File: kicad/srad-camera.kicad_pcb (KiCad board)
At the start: 4 copper layers, 265 parts, among them J1 DEBUG, U1 AP61300Z6, U2 AP61300Z6, U3 RK809-5, U4 STM32U575RGT6, U5 RK3566, U6 MT41K256M16TW-107:P

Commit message: Finished wiring PMIC, STM, power input, IMU, FPC
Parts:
- removed the C43 at (254.5, 70.2)
- removed the C43 at (252.2, 70.5)
- added C43: 22uF, Capacitor_SMD:C_1206_3216Metric, B.Cu at (250.1, 57.5)
- C18, C21, C22, C50, C51: moved to F.Cu
- C2, C20, C3, C38, C39, C4, C40, C41, C42, C44, C45, C49, C5, C52, C53, C54, C55, C56, C57, C58, C59, C60, C61, C62, C63, R30, R33, R34: moved to B.Cu
- moved R1 134.1 mm to (207.0, 69.5), turned to 90 degrees
- moved R2 134.0 mm to (207.1, 65.1), turned to 90 degrees
- moved C128 130.6 mm to (169.0, 101.7)
- moved C129 130.6 mm to (165.5, 101.4)
- moved C130 130.6 mm to (165.5, 103.4)
- moved C131 130.6 mm to (165.5, 105.3)
- moved C132 130.6 mm to (165.5, 107.3)
- moved C133 130.6 mm to (165.5, 109.3)
- moved C134 130.6 mm to (165.5, 111.2)
- moved C135 130.6 mm to (165.5, 113.2)
- moved C136 130.6 mm to (165.5, 115.2)
- moved R49 130.6 mm to (168.4, 103.9)
- moved R3 129.7 mm to (202.5, 75.2), turned to -90 degrees
- moved C53 129.1 mm to (199.8, 67.7), turned to 180 degrees
- moved R32 125.6 mm to (201.5, 75.2), turned to 90 degrees
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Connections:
- C124 pad 2: /RK3566 SoC/VCC_1V8 -> /RK809-5 PMIC/FB4
- C39 pad 1: /RK809-5 PMIC/FB5 -> BUCK5_2V2
- C40 pad 1: /RK809-5 PMIC/FB5 -> BUCK5_2V2
- C41 pad 1: /RK809-5 PMIC/FB5 -> BUCK5_2V2
- C51 pad 2: VCC_3V3_SYS -> /RK809-5 PMIC/VCC_RTC
- L6 pad 2: /RK809-5 PMIC/FB5 -> BUCK5_2V2
- U3 pad 45: VCC_3V3_SYS -> /RK809-5 PMIC/VCC_RTC
- U3 pad 59: /RK809-5 PMIC/FB5 -> BUCK5_2V2
- U5 pad 1C13: /RK3566 SoC/VCC_1V8 -> /RK809-5 PMIC/FB4
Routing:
- net GND: track 34.6 -> 88.8 mm, vias 30 -> 93
- net BUCK5_2V2: track 19.8 -> 56.3 mm, vias 2 -> 5
- net /PMIC_INT: track 7.44 -> 26.2 mm, vias 1 -> 2
- net /PMIC_CLK: track 1.77 -> 20.1 mm, vias 1 -> 0
- net /PMIC_SDA: track 5.60 -> 23.1 mm
- net /RK809-5 PMIC/FB4: track 0.00 -> 17.2 mm, vias 0 -> 2
- net /PMIC_SCL: track 6.08 -> 22.6 mm
- net /RK809-5 PMIC/VBUCK3: track 6.47 -> 21.4 mm, vias 0 -> 3
- net /STM32U575RGT6/SWDIO: track 16.6 -> 3.29 mm
- net /STM32U575RGT6/SWO: track 11.3 -> 1.86 mm
- net /RK3566 SoC/VCCA_1V8_PMU: track 1.69 -> 10.5 mm, vias 0 -> 1
- net /STM32U575RGT6/SWCLK: track 10.6 -> 1.97 mm
- net /Power Supply/VIN_5V: track 17.1 -> 8.90 mm, vias 0 -> 4
- net VCCIO_3V3_IMU: track 15.3 -> 8.29 mm, vias 1 -> 3
- net /LSM6DSRTR/SDA: track 11.3 -> 4.46 mm, vias 2 -> 1
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- added copper zone on B.Cu, net GND
- added copper zone on F.Cu, net GND

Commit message: WIP PCB layout
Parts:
- removed D1: SMAJ5.0A, Diode_SMD:D_SMA
- added H1: MntHole, srad-camera-footprints:4-40_MountingHole, F.Cu at (125.0, 80.5)
- added H2: MntHole, srad-camera-footprints:4-40_MountingHole, F.Cu at (167.0, 80.5)
- added H3: MntHole, srad-camera-footprints:4-40_MountingHole, F.Cu at (125.0, 122.5)
- added H4: MntHole, srad-camera-footprints:4-40_MountingHole, F.Cu at (167.0, 122.5)
- added SW1: POWER, Button_Switch_SMD:SW_SPDT_PCM12, F.Cu at (66.0, 61.1)
- added SW2: USER, Button_Switch_SMD:SW_SPST_EVQP2_MiddlePushTravel_H2.5mm, F.Cu at (65.1, 74.5)
- added SW3: BOOT0, Button_Switch_SMD:SW_SPDT_PCM12, F.Cu at (66.0, 68.0)
- C1, FB1, FPC1, IMU1, R6, R7, SD1: moved to B.Cu
- C62, C63, R33, R34: moved to F.Cu
- J1: footprint Connector_PinHeader_1.27mm:PinHeader_2x05_P1.27mm_Vertical_SMD -> Connector_PinHeader_1.27mm:PinHeader_2x03_P1.27mm_Vertical
- USB1: footprint srad-camera-footprints:USB-SMD_TYPE-C16PIN-1 -> Connector_USB:USB_C_Receptacle_G-Switch_GT-USB-7010ASV
- moved C10 113.9 mm to (149.2, 85.5)
- moved C13 113.9 mm to (149.6, 83.0)
- moved C17 113.9 mm to (151.2, 93.9)
- moved C30 113.9 mm to (151.3, 92.7)
- moved L4 113.9 mm to (153.9, 85.6)
- moved R21 113.9 mm to (151.2, 92.0)
- moved R22 113.9 mm to (152.9, 83.2)
- moved R23 113.9 mm to (154.4, 83.2)
- moved C11 113.9 mm to (143.3, 86.8)
- moved C12 113.9 mm to (150.2, 88.0)
- moved C14 113.9 mm to (143.5, 88.6)
- moved C15 113.9 mm to (143.3, 85.1)
- moved C16 113.9 mm to (143.9, 83.4)
- moved C18 113.9 mm to (144.5, 92.6)
- moved C19 113.9 mm to (143.1, 94.1)
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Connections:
- net /RK3566 SoC/MIPI_DN0 renamed /RK3566 SoC/MIPI_D0_N
- net /RK3566 SoC/MIPI_DN1 renamed /RK3566 SoC/MIPI_D1_N
- net /RK3566 SoC/MIPI_DN2 renamed /RK3566 SoC/MIPI_D2_N
- net /RK3566 SoC/MIPI_DN3 renamed /RK3566 SoC/MIPI_D3_N
- net /RK3566 SoC/MIPI_DP0 renamed /RK3566 SoC/MIPI_D0_P
- net /RK3566 SoC/MIPI_DP1 renamed /RK3566 SoC/MIPI_D1_P
- net /RK3566 SoC/MIPI_DP2 renamed /RK3566 SoC/MIPI_D2_P
- net /RK3566 SoC/MIPI_DP3 renamed /RK3566 SoC/MIPI_D3_P
- D4 pad 1: Net-(D4-A1) -> GND
- D5 pad 1: Net-(D4-A1) -> GND
- D6 pad 1: Net-(D4-A1) -> GND
- D7 pad 1: Net-(D4-A1) -> GND
- D8 pad 1: Net-(D4-A1) -> GND
- D9 pad 1: Net-(D4-A1) -> GND
- FB2 pad 2: USB_5V -> VBUS_5V
- J1 pad 1: /STM32U575RGT6/VDD_3V3 -> GND
- J1 pad 2: Net-(J1-Pin_2) -> /STM32U575RGT6/VDD_3V3
- J1 pad 3: GND -> /STM32U575RGT6/NRST
- J1 pad 4: Net-(J1-Pin_4) -> /STM32U575RGT6/SWO
- J1 pad 5: GND -> Net-(J1-SWCLK)
- J1 pad 6: /STM32U575RGT6/SWO -> Net-(J1-SWDIO)
- R14 pad 1: Net-(USB1-CC2) -> Net-(USB1-CC1)
- R15 pad 1: GND -> Net-(USB1-CC2)
- R15 pad 2: Net-(USB1-CC1) -> GND
- R19 pad 2: USB_5V -> VBUS_5V
- R4 pad 1: /STM32U575RGT6/SWDIO -> /STM32U575RGT6/SWCLK
- R4 pad 2: Net-(J1-Pin_2) -> Net-(J1-SWCLK)
- R5 pad 1: /STM32U575RGT6/SWCLK -> /STM32U575RGT6/SWDIO
- R5 pad 2: Net-(J1-Pin_4) -> Net-(J1-SWDIO)
- USB1 pad A8: unconnected-(USB1-SBU1-PadA8) -> (no net)
- USB1 pad B8: unconnected-(USB1-SBU2-PadB8) -> (no net)
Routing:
- net GND: track 88.8 -> 110.9 mm, vias 93 -> 234
- net Net-(USB1-SHIELD): track 0.00 -> 19.4 mm, vias 0 -> 3
- net /RK3566 SoC/MIPI_D2_P: track 0.00 -> 14.8 mm, vias 0 -> 1
- net /RK3566 SoC/MIPI_D0_P: track 0.00 -> 14.3 mm, vias 0 -> 1
- net /RK3566 SoC/MIPI_D2_N: track 0.00 -> 14.2 mm
- net /RK3566 SoC/MIPI_D3_P: track 0.00 -> 14.2 mm, vias 0 -> 1
- net /RK3566 SoC/MIPI_CN: track 0.00 -> 14.2 mm, vias 0 -> 2
- net VCC_3V3_SD: track 4.41 -> 17.7 mm, vias 0 -> 3
- net /RK3566 SoC/MIPI_D1_N: track 0.00 -> 12.9 mm
- net (no net): track 12.6 -> 0.00 mm
- net /RK3566 SoC/MIPI_CP: track 0.00 -> 12.5 mm, vias 0 -> 2
- net /RK3566 SoC/MIPI_D1_P: track 0.00 -> 12.4 mm, vias 0 -> 1
- net /RK3566 SoC/MIPI_D0_N: track 0.00 -> 12.0 mm
- net /RK3566 SoC/MIPI_D3_N: track 0.00 -> 11.4 mm
- net /RK3566 SoC/CAM_GPIO1: track 0.00 -> 11.4 mm, vias 0 -> 1
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- added copper zone on In2.Cu, net GND
- removed copper zone on F.Cu, net GND
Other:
- board text removed: "SCREWS!!!!!"

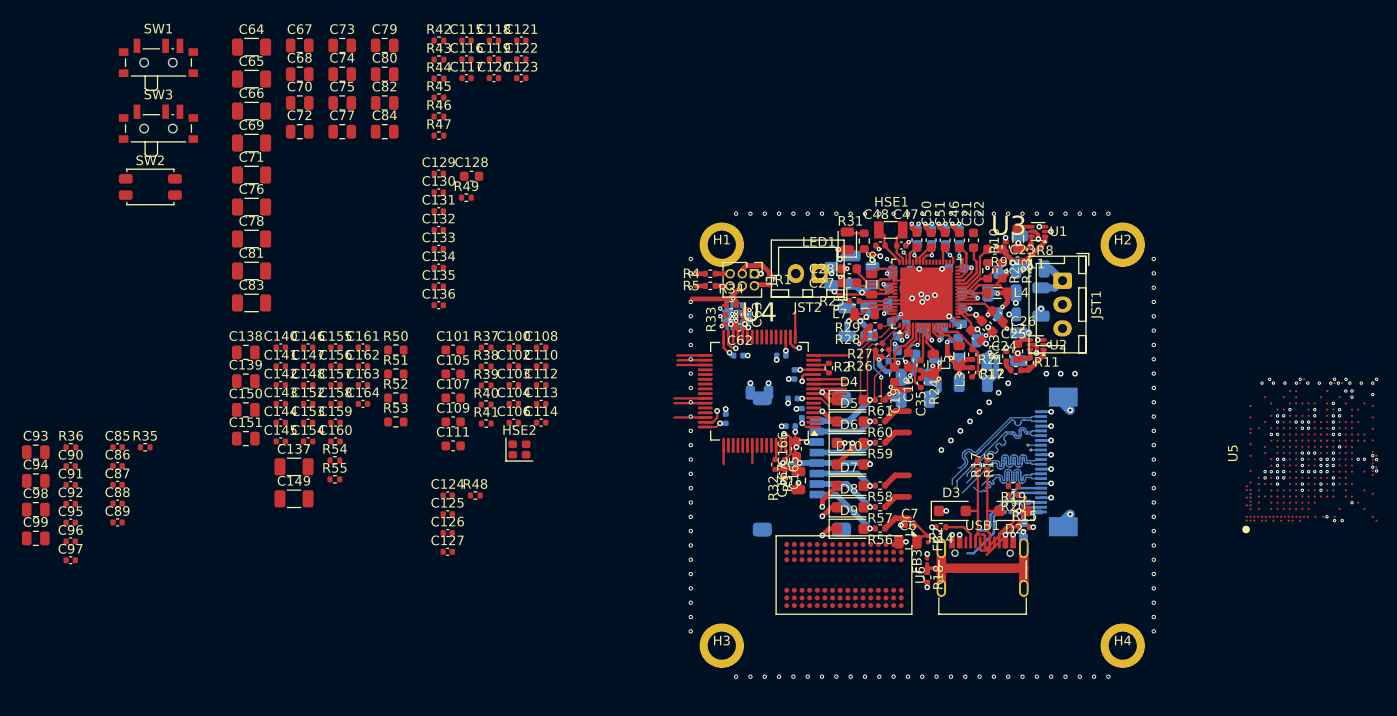
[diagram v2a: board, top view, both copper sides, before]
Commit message: All major components placed on board
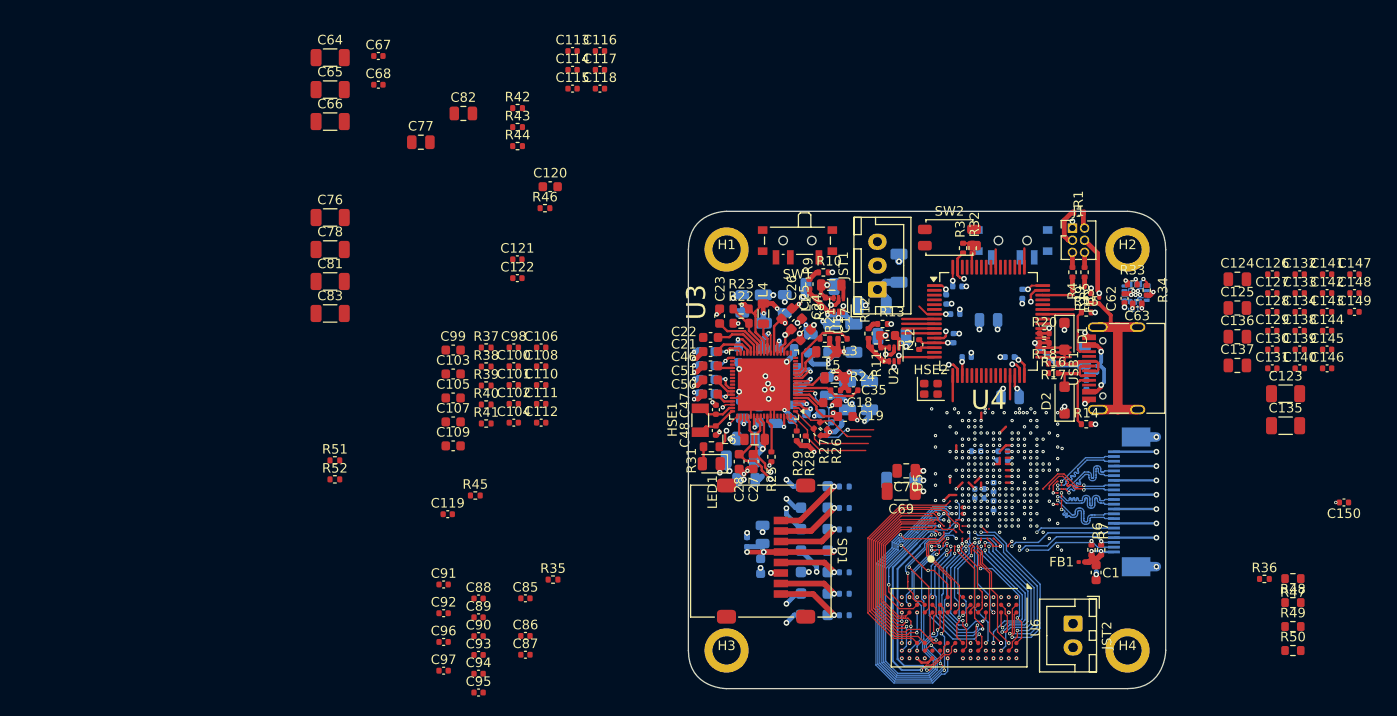
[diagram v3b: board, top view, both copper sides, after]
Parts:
- removed the C115 at (98.3, 59.1)
- removed the C116 at (98.3, 61.1)
- removed the C117 at (98.3, 63.0)
- removed the C124 at (96.3, 106.8)
- removed the C126 at (96.3, 110.7)
- removed the C127 at (96.3, 112.7)
- removed the C129 at (95.3, 73.0)
- removed the C130 at (95.3, 75.0)
- removed the C131 at (95.3, 77.0)
- removed the C132 at (95.3, 79.0)
- removed the C135 at (95.3, 84.9)
- removed the C136 at (95.3, 86.8)
- removed C42, C43: 22uF, Capacitor_SMD:C_1206_3216Metric
- removed the C85 at (61.7, 101.7)
- removed the C87 at (61.7, 105.7)
- removed L7: 470nH / 4A, Inductor_SMD:L_0805_2012Metric
- removed the R42 at (95.4, 59.1)
- removed the R43 at (95.4, 61.1)
- removed the R44 at (95.4, 63.1)
- C1, FB1, R6, R7, SD1: moved to F.Cu
- C151: renamed from C165; moved to B.Cu
- C152: renamed from C166; moved to B.Cu
- C153: renamed from C167; moved to B.Cu
- C6, C7, C71, FB2, SW3: moved to B.Cu
- C67, C68: footprint Capacitor_SMD:C_0805_2012Metric -> Capacitor_SMD:C_0402_1005Metric
- C72, C73, C74, C75, C79, C80, C84: footprint Capacitor_SMD:C_0805_2012Metric -> Capacitor_SMD:C_0402_1005Metric; moved to B.Cu
- C91: renamed from C93; footprint Capacitor_SMD:C_0805_2012Metric -> Capacitor_SMD:C_0402_1005Metric
- C92: renamed from C94; footprint Capacitor_SMD:C_0805_2012Metric -> Capacitor_SMD:C_0402_1005Metric
- C96: renamed from C98; footprint Capacitor_SMD:C_0805_2012Metric -> Capacitor_SMD:C_0402_1005Metric
- C97: renamed from C99; footprint Capacitor_SMD:C_0805_2012Metric -> Capacitor_SMD:C_0402_1005Metric
- D3: renamed from D4; moved to B.Cu
- D4: renamed from D5; moved to B.Cu
- D5: renamed from D6; moved to B.Cu
- D6: renamed from D7; moved to B.Cu
- D7: renamed from D8; moved to B.Cu
- D8: renamed from D9; moved to B.Cu
- D9: renamed from D10; moved to B.Cu
- R53: renamed from R56; moved to B.Cu
- R54: renamed from R57; moved to B.Cu
- R55: renamed from R58; moved to B.Cu
- R56: renamed from R59; moved to B.Cu
- R57: renamed from R60; moved to B.Cu
- R58: renamed from R61; moved to B.Cu
- USB1: footprint Connector_USB:USB_C_Receptacle_G-Switch_GT-USB-7010ASV -> Connector_USB:USB_C_Receptacle_HRO_TYPE-C-31-M-12
- moved R36 125.8 mm to (181.8, 115.5)
- moved C123 104.1 mm to (184.1, 96.1)
- moved C135 104.1 mm to (184.1, 99.5)
- moved C147 104.1 mm to (191.3, 83.6)
- moved C148 104.1 mm to (191.3, 85.6)
- moved C149 104.1 mm to (191.3, 87.5)
- moved C124 104.1 mm to (179.0, 84.1)
- moved C125 104.1 mm to (179.0, 87.1)
- moved C126 104.1 mm to (182.7, 83.6)
- moved C127 104.1 mm to (182.7, 85.6)
- moved C128 104.1 mm to (182.7, 87.5)
- moved C129 104.1 mm to (182.7, 89.5)
- moved C130 104.1 mm to (182.7, 91.5)
- moved C131 104.1 mm to (182.7, 93.4)
- moved C132 104.1 mm to (185.5, 83.6)
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- renumbered C102 to C100, C103 to C101, C104 to C102, C105 to C103, C106 to C104, C107 to C105, C108 to C106, C109 to C107, C110 to C108, C111 to C109, C112 to C110, C113 to C111, C114 to C112, C118 to C113, C119 to C114, C120 to C115, C121 to C116, C122 to C117, C123 to C118, C125 to C119, C128 to C120, C133 to C121, C134 to C122, C137 to C123, C138 to C124, C139 to C125, C140 to C126, C141 to C127, C142 to C128, C143 to C129, C144 to C130, C145 to C131, C146 to C132, C147 to C133, C148 to C134, C149 to C135, C150 to C136, C151 to C137, C152 to C138, C153 to C139, C154 to C140, C155 to C141, C156 to C142, C157 to C143, C158 to C144, C159 to C145, C160 to C146, C161 to C147, C162 to C148, C163 to C149, C164 to C150, C86 to C85, C88 to C86, C89 to C87, C90 to C88, C91 to C89, C92 to C90, C95 to C93, C96 to C94, C97 to C95, C100 to C98, C101 to C99, D2 to D1, D3 to D2, R19 to R18, R18 to R19, R45 to R42, R46 to R43, R47 to R44, R48 to R45, R49 to R46, R50 to R47, R51 to R48, R52 to R49, R53 to R50, R54 to R51, R55 to R52
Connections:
- R18 pad 2: VBUS_5V -> /Power Supply/VIN_5V
- U3 pad 64: /RK809-5 PMIC/FB4 -> unconnected-(U3-FB4-Pad64)
- U3 pad 65: /RK809-5 PMIC/SW4 -> unconnected-(U3-SW4-Pad65)
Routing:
- net VCC_DDR: track 0.00 -> 95.6 mm, vias 8 -> 31
- net GND: track 110.9 -> 164.2 mm, vias 234 -> 285
- net /MT41K256 DDR3L/CSn0: track 0.00 -> 39.3 mm, vias 0 -> 2
- net /MT41K256 DDR3L/BA2: track 0.00 -> 35.8 mm, vias 0 -> 2
- net /MT41K256 DDR3L/BA1: track 0.00 -> 33.2 mm, vias 1 -> 4
- net /MT41K256 DDR3L/BA0: track 0.00 -> 32.9 mm, vias 0 -> 2
- net /MT41K256 DDR3L/WEn: track 0.00 -> 31.9 mm, vias 0 -> 2
- net /MT41K256 DDR3L/CKE: track 0.00 -> 28.8 mm, vias 0 -> 2
- net /MT41K256 DDR3L/A2: track 0.00 -> 27.6 mm, vias 0 -> 2
- net /MT41K256 DDR3L/A10: track 0.00 -> 25.0 mm
- net /MT41K256 DDR3L/A1: track 0.00 -> 24.5 mm, vias 1 -> 0
- net /MT41K256 DDR3L/A12: track 0.00 -> 23.8 mm
- net /MT41K256 DDR3L/CK_N: track 0.00 -> 23.8 mm, vias 0 -> 2
- net /MT41K256 DDR3L/CK_P: track 0.00 -> 22.6 mm, vias 0 -> 2
- net /MT41K256 DDR3L/A8: track 0.00 -> 20.8 mm, vias 0 -> 2
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- added copper zone on In2.Cu, net VCC_DDR
- removed copper zone on In2.Cu, net GND
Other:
- board outline added: 50 x 50 mm
